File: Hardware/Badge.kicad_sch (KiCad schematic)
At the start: 91 parts, among them J1 BATT_CON, J2 BATT_CON, J3 BATT_CON, J4 Conn_02x15_Counter_Clockwise, J6 Internal_I2C, P1 PWR_N_DATA, P3 PWR_N_DATA, P4 PWR_N_DATA, Q1 SI1967DH-T1-GE3, Q2 2SC4213, Q3 PMOS, SW1 BOOT_MODE, SW2 RESET, SW3 BATT_PWR, SW5 Button B, SW6 Button A, SW8 BATT_PWR, SW9 BATT_PWR, U1 W25Q128JVS, U2 MCP73832-2-OT, U3 LD1117S33TR_SOT223, U4 RP2040, U8 TP4057, U9 TP4057, X1 SAO_v2, Y1 12MHz_GND24

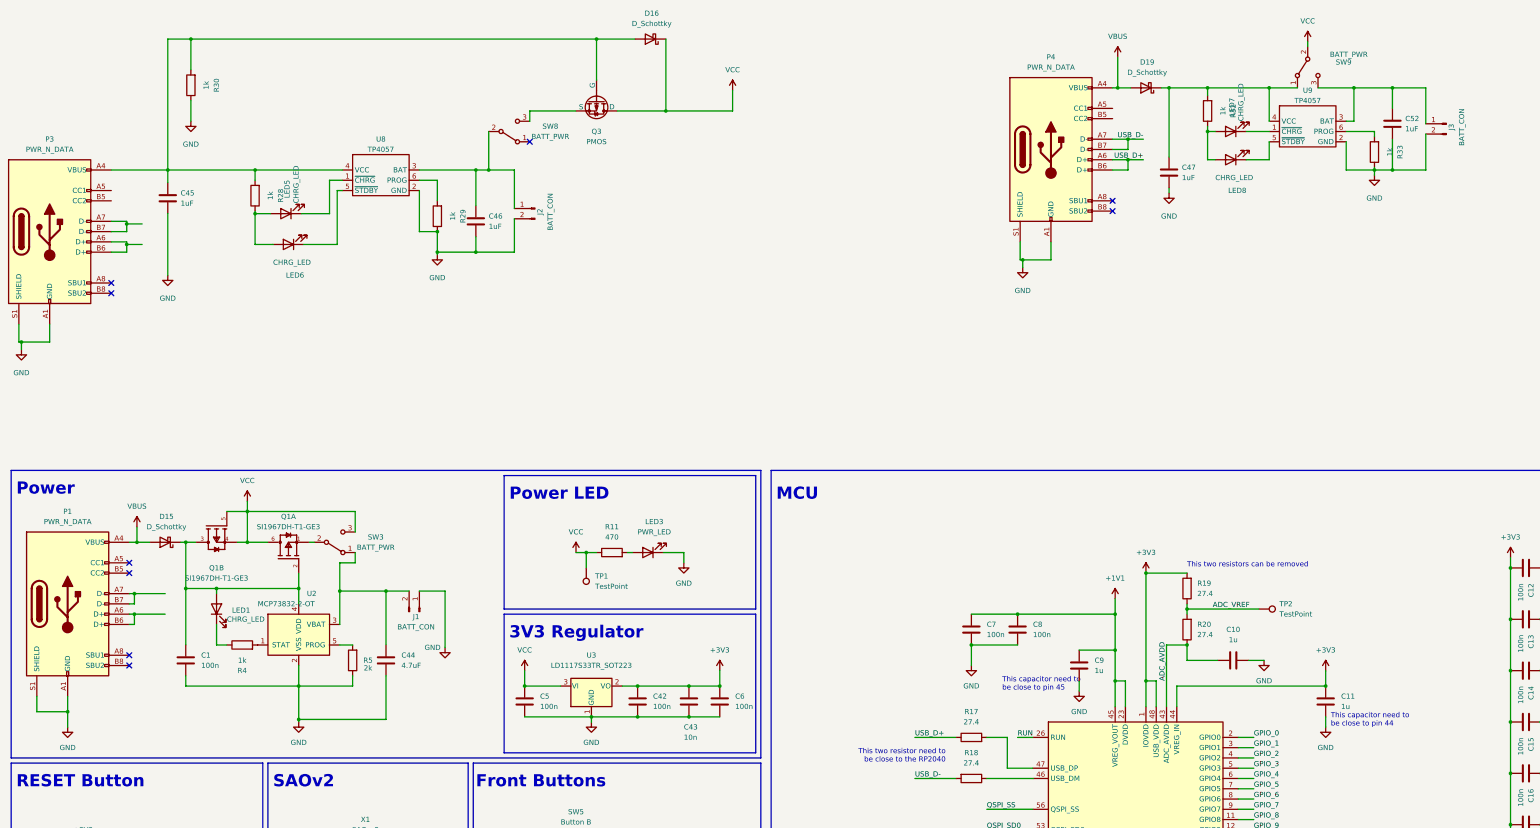
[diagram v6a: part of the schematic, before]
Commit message: Ready to order - THE POWER DIODE IS MISSING (need futher investigations)
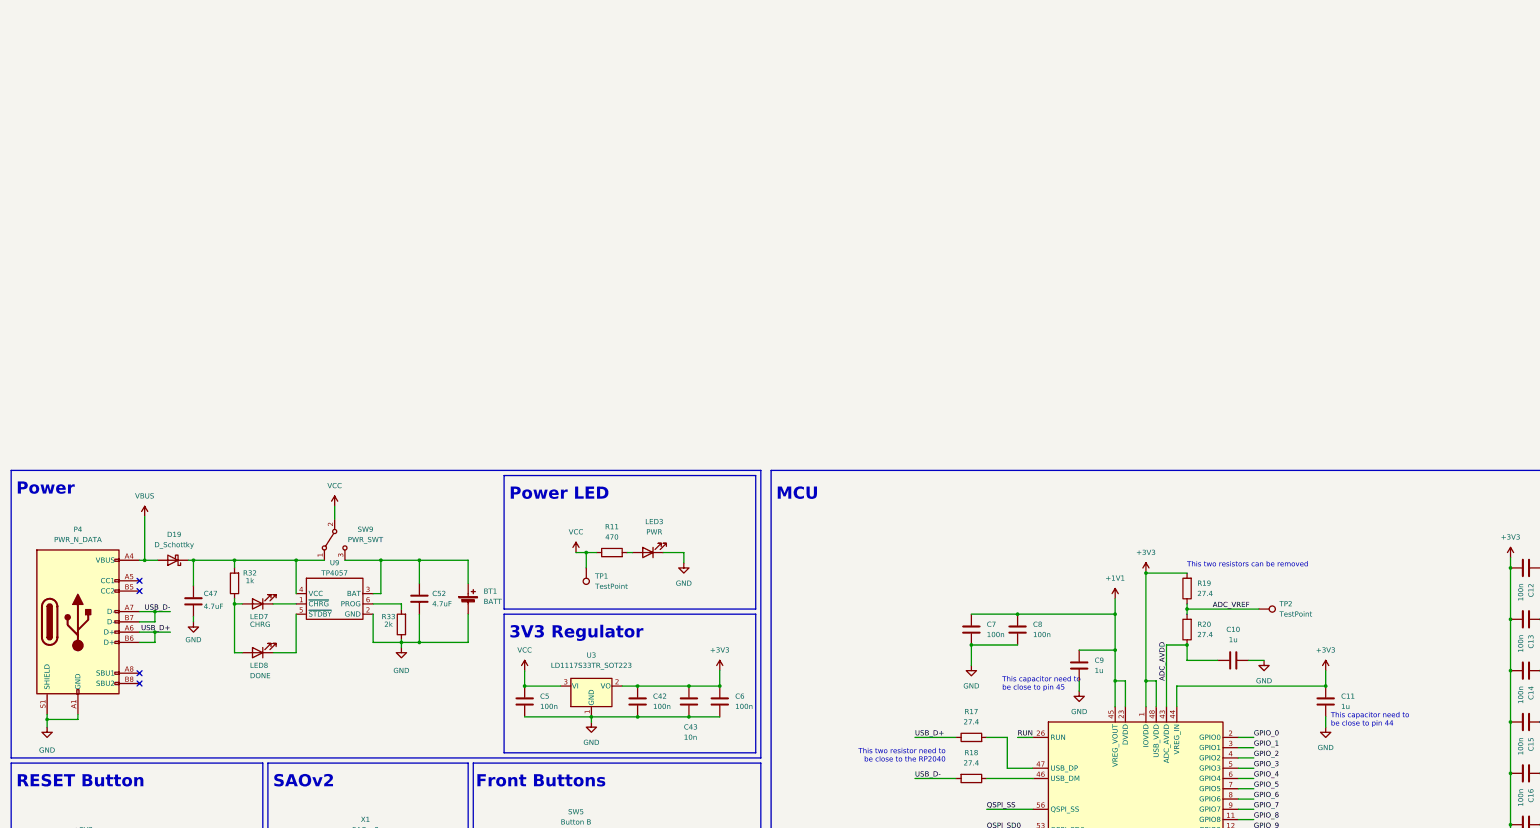
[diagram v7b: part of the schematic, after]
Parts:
- removed C1: 100n, Capacitor_SMD:C_0402_1005Metric, symbol Device:C
- removed C44: 4.7uF, Capacitor_SMD:C_0402_1005Metric, symbol Device:C
- removed C45, C46: 1uF, Capacitor_SMD:C_0402_1005Metric, symbol Device:C
- removed D15, D16: D_Schottky, Diode_SMD:D_SMA, symbol Device:D_Schottky
- removed J1, J2, J3: BATT_CON, Connector_JST:JST_PH_B2B-PH-K_1x02_P2.00mm_Vertical, symbol Connector:Conn_01x02_Male
- removed LED1, LED5, LED6: CHRG_LED, LED_SMD:LED_0603_1608Metric, symbol Device:LED
- removed P1, P3: PWR_N_DATA, Connector_USB:USB_C_Receptacle_Palconn_UTC16-G, symbol Connector:USB_C_Receptacle_USB2.0
- removed Q1: SI1967DH-T1-GE3, SI1967DH:Vishay-S-03946-07_2001-B-0, symbol Tran SI1967DH-T1-GE3:SI1967DH-T1-GE3
- removed Q3: PMOS, symbol Simulation_SPICE:PMOS
- removed R28, R29, R30, R4: 1k, Resistor_SMD:R_0402_1005Metric, symbol Device:R
- removed R5: 2k, Resistor_SMD:R_0402_1005Metric, symbol Device:R
- removed SW3, SW8: BATT_PWR, Button_Switch_SMD:SW_SPDT_CK-JS102011SAQN, symbol Switch:SW_SPDT
- removed U2: MCP73832-2-OT, Package_TO_SOT_SMD:SOT-23-5, symbol Battery_Management:MCP73832-2-OT
- removed U8: TP4057, Package_TO_SOT_SMD:SOT-23-6, symbol TP4057:tp4057
- added BT1: BATT, Connector_JST:JST_PH_B2B-PH-K_1x02_P2.00mm_Vertical, symbol Device:Battery_Cell
- C47, C52: value 1uF -> 4.7uF
- LED3: value PWR_LED -> PWR
- LED7: value CHRG_LED -> CHRG
- LED8: value CHRG_LED -> DONE
- R33: value 1k -> 2k
- SW9: value BATT_PWR -> PWR_SWT
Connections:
- net GND: now also BT1.2 (-)
- net at C52.1, SW9.3 (C), U9.3 (BAT): now also BT1.1 (+)
- no-connect marks 11 -> 6
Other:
- moved on the sheet: C47, C52, D19, LED7, LED8, P4, R32, R33, SW9, U9

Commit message: Reworked the power system - ORDERED ON JLCPCB
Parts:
- removed D19: D_Schottky, Diode_SMD:D_SMA, symbol Device:D_Schottky
- removed P4: PWR_N_DATA, Connector_USB:USB_C_Receptacle_Palconn_UTC16-G, symbol Connector:USB_C_Receptacle_USB2.0
- removed U3: LD1117S33TR_SOT223, Package_TO_SOT_SMD:SOT-223-3_TabPin2, symbol Regulator_Linear:LD1117S33TR_SOT223
- added D18: DNP, Diode_SMD:D_SMA, symbol Device:D_Schottky
- added L1: 2.2uH, Inductor_SMD:L_0805_2012Metric, symbol Device:L
- added P1: PWR_N_DATA, Connector_USB:USB_C_Receptacle_Palconn_UTC16-G, symbol Connector:USB_C_Receptacle_USB2.0
- added R30: 100k, Resistor_SMD:R_0402_1005Metric, symbol Device:R
- added R31: 4.7k, Resistor_SMD:R_0402_1005Metric, symbol Device:R
- added U2: AMS1117-3.3, Package_TO_SOT_SMD:SOT-223-3_TabPin2, symbol Regulator_Linear:AMS1117-3.3
- added U8: SY6280AAC, Package_TO_SOT_SMD:SOT-23-5, symbol mch2021-rescue:AAT4610BIGV-1-T1-Power_Management
- TP1: value TestPoint -> VCC
- TP2: value TestPoint -> VREF
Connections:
- net +3V3: now also L1.1; no longer C42.2
- net GND: now also P1.A1 (GND), P1.A12 (GND), P1.B1 (GND), P1.B12 (GND), P1.S1 (SHIELD), R30.1, R31.1, U2.1 (GND), U8.2 (GND)
- net USB_D+: now also P1.A6 (D+), P1.B6 (D+)
- net USB_D-: now also P1.A7 (D-), P1.B7 (D-)
- net VBUS: now also C47.1, R32.2, U9.4 (VCC), D18.2 (A), P1.A4 (VBUS), P1.A9 (VBUS), P1.B4 (VBUS), P1.B9 (VBUS)
- net VCC: now also D18.1 (K), U2.3 (VI), U8.1 (OUT); no longer SW9.2 (B)
- net at BT1.1 (+), C52.1, U9.3 (BAT): now also SW9.2 (B), U8.5 (IN); no longer SW9.3 (C)
- new net: R31.2, U8.3 (SET)
- new net: R30.2, SW9.1 (A), U8.4 (ON)
- new net: C42.2, L1.2, U2.2 (VO)
- no-connect marks 6 -> 7
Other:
- note added: "Iset = 1.44A = 6800 / 4700"
- note added: "Power switch"
- moved on the sheet: BT1, C42, C43, C47, C5, C52, C6, LED3, LED7, LED8, R11, R32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
